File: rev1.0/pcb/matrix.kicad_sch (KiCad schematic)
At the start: 103 parts

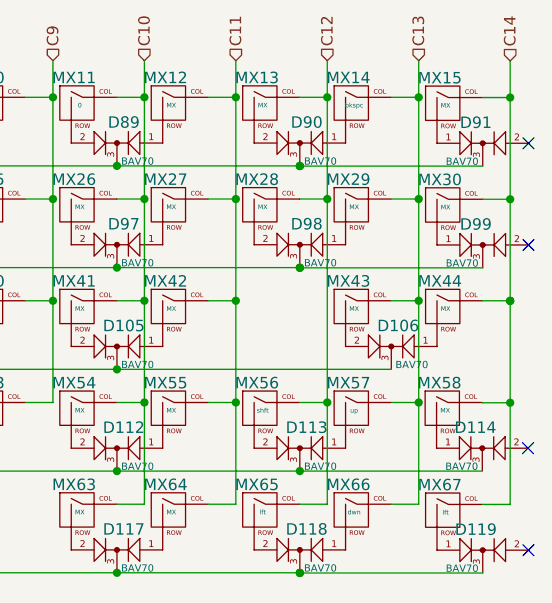
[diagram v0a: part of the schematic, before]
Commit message: rp2040 port: updated schematic and fixed footprints
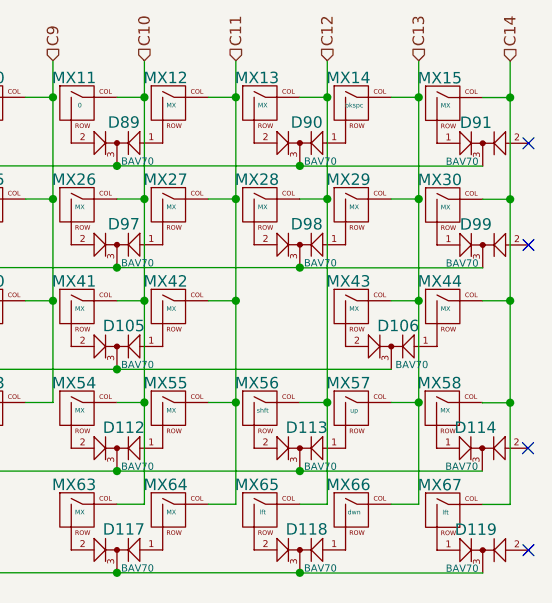
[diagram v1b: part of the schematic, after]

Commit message: fixup and add prod
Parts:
- D100, D101, D102, D103, D104, D105, D106, D107, D108, D109, D110, D111, D112, D113, D114, D115, D116, D117, D118, D119, D84, D85, D86, D87, D88, D89, D90, D91, D92, D93, D94, D95, D96, D97, D98, D99: JLCPCB_CORRECTION (none) -> 0; 0; 180; LCSC (none) -> C2501
- MX1, MX10, MX11, MX12, MX13, MX14, MX15, MX16, MX17, MX18, MX19, MX2, MX20, MX21, MX22, MX23, MX24, MX25, MX26, MX27, MX28, MX29, MX3, MX30, MX31, MX32, MX33, MX34, MX35, MX36, MX37, MX38, MX39, MX4, MX40, MX41, MX42, MX43, MX44, MX45, MX46, MX47, MX48, MX49, MX5, MX50, MX51, MX52, MX53, MX54, MX55, MX56, MX57, MX58, MX59, MX6, MX60, MX61, MX62, MX63, MX64, MX65, MX66, MX67, MX7, MX8, MX9: LCSC (none) -> C5156480
